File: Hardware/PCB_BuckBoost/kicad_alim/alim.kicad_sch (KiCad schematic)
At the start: 36 parts, among them J1 Conn_01x02, J2 Conn_01x02, J3 Conn_01x02, J4 Conn_01x02, U1 MIC3172YM, U2 MIC3172YM

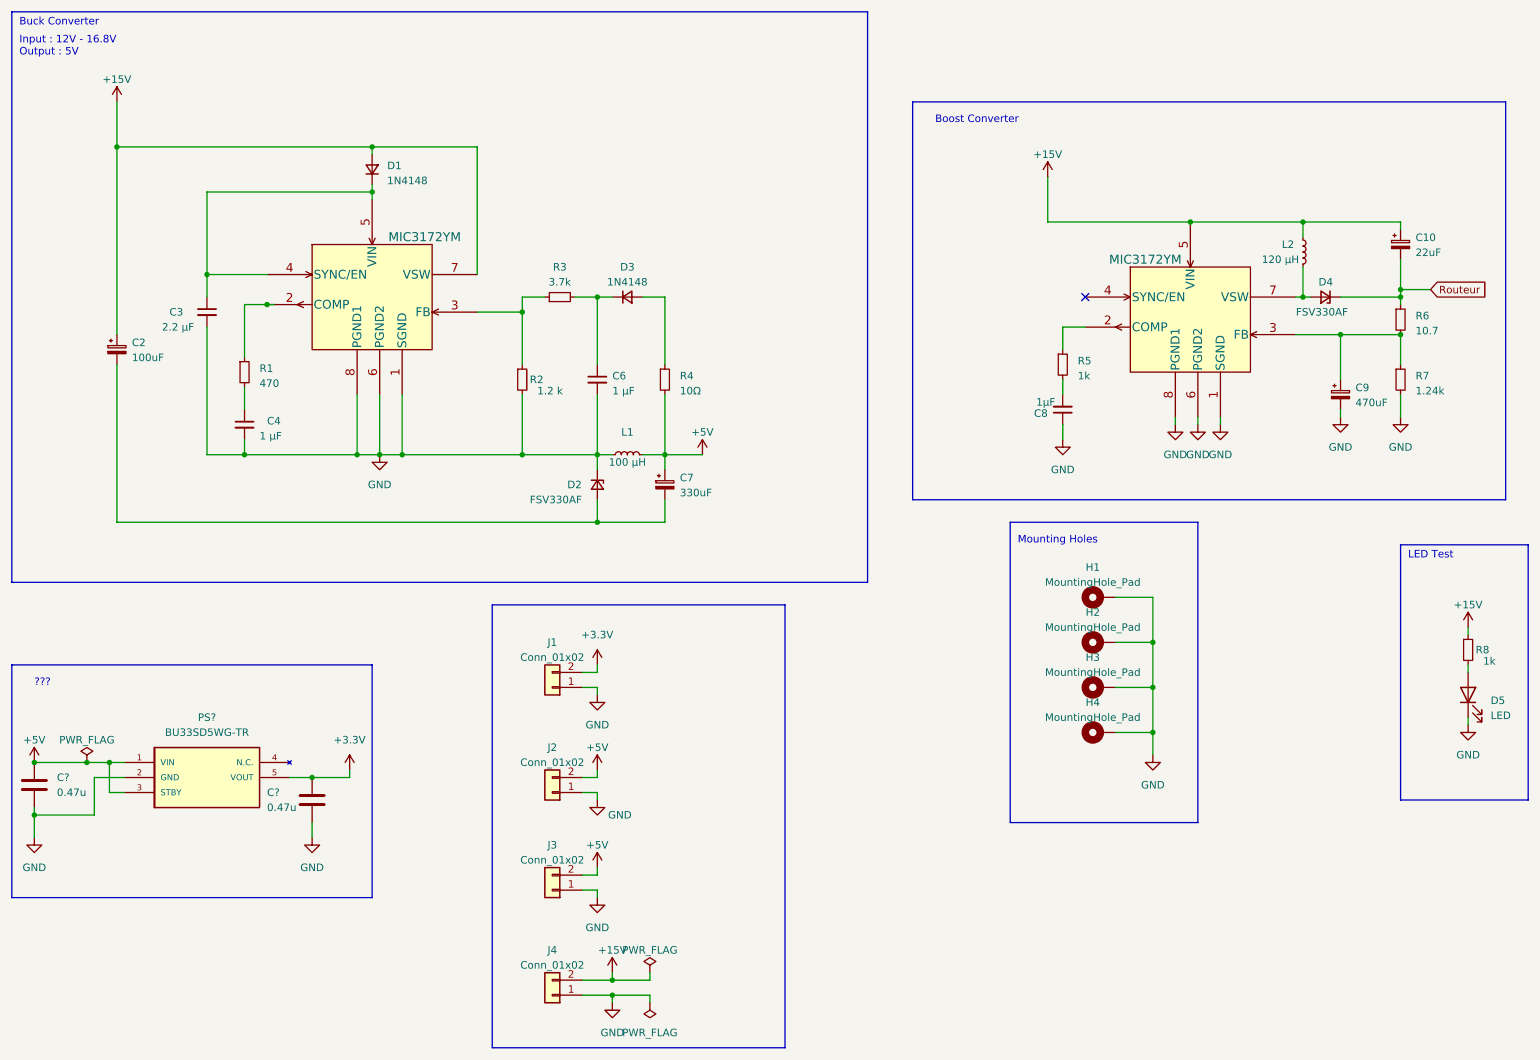
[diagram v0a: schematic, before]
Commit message: changement du schéma Buck/Boost car erreur
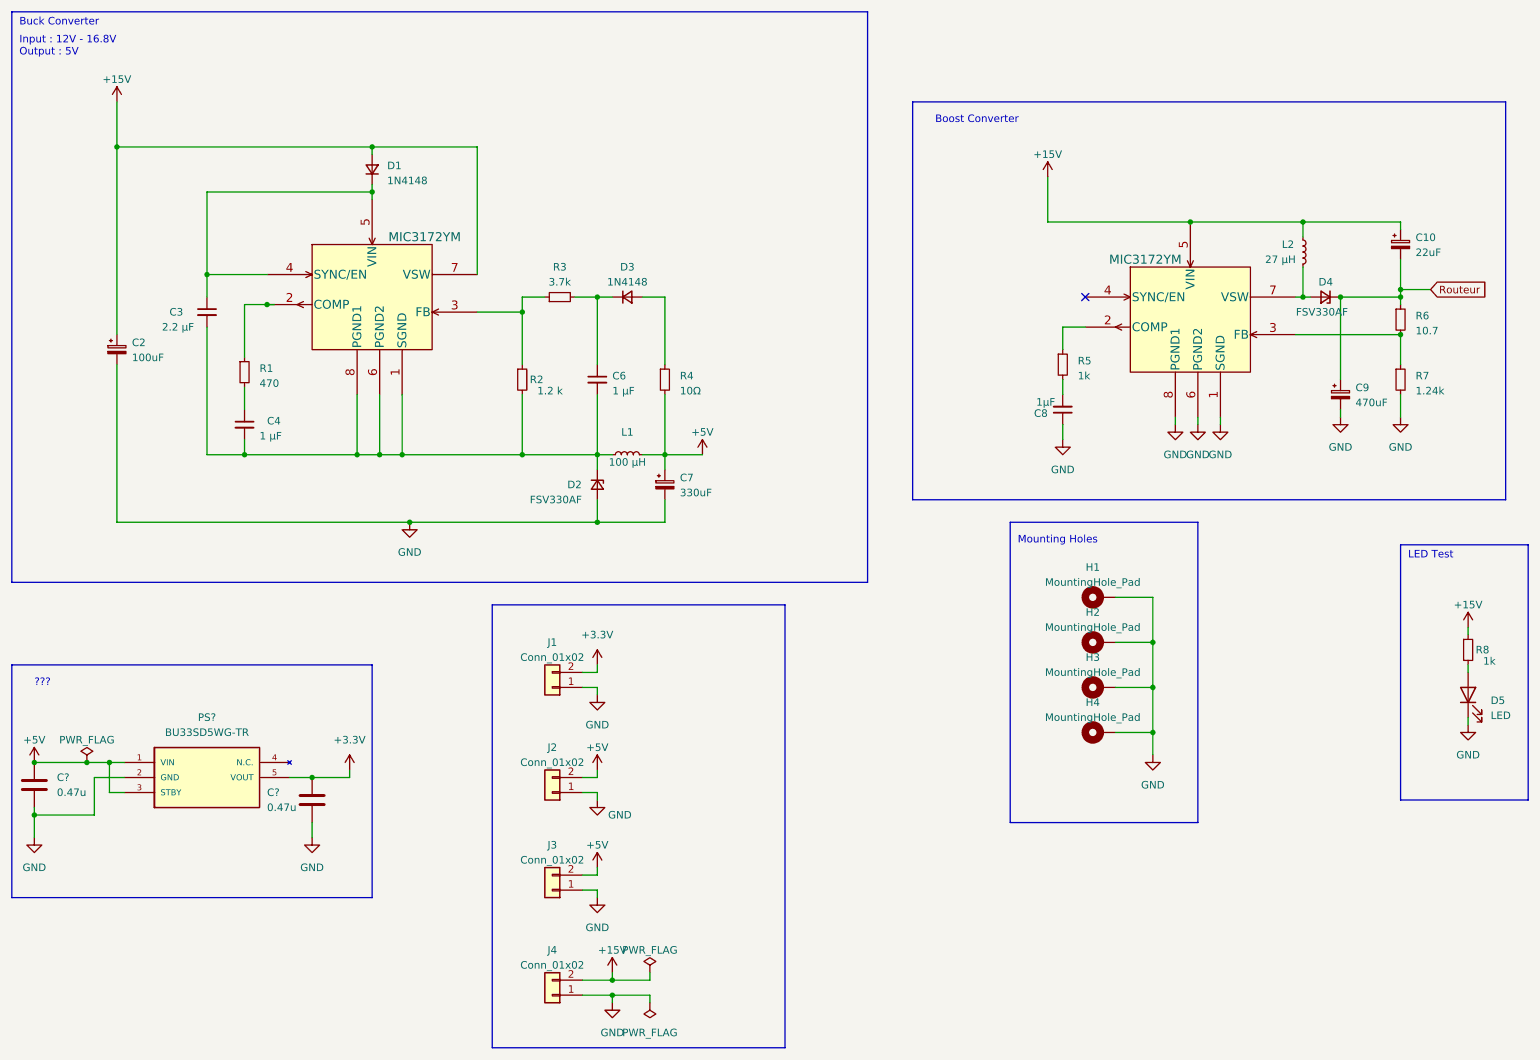
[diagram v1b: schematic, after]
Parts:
- L2: value 120 µH -> 27 µH
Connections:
- net GND: now also C2.2, C7.2, D2.2 (A); no longer C3.2, C4.2, C6.2, D2.1 (K), L1.1, R2.2, U1.1 (SGND), U1.6 (PGND2), U1.8 (PGND1)
- net Routeur: now also C9.1
- net at R6.2, R7.1, U2.3 (FB): no longer C9.1
- new net: C3.2, C4.2, C6.2, D2.1 (K), L1.1, R2.2, U1.1 (SGND), U1.6 (PGND2), U1.8 (PGND1)
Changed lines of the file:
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@@
   (junction (at 114.3 69.85) (diameter 0) (color 0 0 0 0)
   )
-  (junction (at 240.03 76.2) (diameter 0) (color 0 0 0 0)
-  )
   (junction (at 250.19 68.58) (diameter 0) (color 0 0 0 0)
   )
@@
   (junction (at 76.2 52.07) (diameter 0) (color 0 0 0 0)
   )
+  (junction (at 82.55 107.95) (diameter 0) (color 0 0 0 0)
+  )
   (junction (at 58.42 71.12) (diameter 0) (color 0 0 0 0)
   )
@@
   )
   (junction (at 27.94 148.59) (diameter 0) (color 0 0 0 0)
+  )
+  (junction (at 240.03 69.85) (diameter 0) (color 0 0 0 0)
   )
   (junction (at 77.47 96.52) (diameter 0) (color 0 0 0 0)
@@
     (stroke (width 0) (type default))
   )
-  (wire (pts (xy 240.03 76.2) (xy 250.19 76.2))
-    (stroke (width 0) (type default))
-  )
   (wire (pts (xy 193.04 91.44) (xy 193.04 93.98))
     (stroke (width 0) (type default))
@@
     (stroke (width 0) (type default))
   )
-  (wire (pts (xy 240.03 83.82) (xy 240.03 76.2))
-    (stroke (width 0) (type default))
-  )
   (wire (pts (xy 27.94 148.59) (xy 31.75 148.59))
     (stroke (width 0) (type default))
@@
     (stroke (width 0) (type default))
   )
+  (wire (pts (xy 240.03 69.85) (xy 240.03 83.82))
+    (stroke (width 0) (type default))
+  )
+  (wire (pts (xy 82.55 107.95) (xy 114.3 107.95))
+    (stroke (width 0) (type default))
+  )
   (wire (pts (xy 48.26 52.07) (xy 76.2 52.07))
     (stroke (width 0) (type default))
@@
     (stroke (width 0) (type default))
   )
-  (wire (pts (xy 232.41 76.2) (xy 240.03 76.2))
+  (wire (pts (xy 232.41 76.2) (xy 250.19 76.2))
     (stroke (width 0) (type default))
   )
@@
     (stroke (width 0) (type default))
   )
-  (wire (pts (xy 33.02 107.95) (xy 114.3 107.95))
+  (wire (pts (xy 33.02 107.95) (xy 82.55 107.95))
     (stroke (width 0) (type default))
   )
@@
       (effects (font (size 1.27 1.27)))
     )
-    (property "Value" "120 µH" (at 229.87 63.5 0)
+    (property "Value" "27 µH" (at 229.87 63.5 0)
       (effects (font (size 1.27 1.27)))
     )
@@
         (path "/9ea535e2-254b-400e-a1b3-21cc38003798"
           (reference "#PWR01") (unit 1)
-        )
-      )
-    )
-  )
-  (symbol (lib_id "power:GND") (at 77.47 96.52 0) (unit 1)
-    (in_bom yes) (on_board yes) (dnp no) (fields_autoplaced)
-    (property "Reference" "#PWR06" (at 77.47 102.87 0)
-      (effects (font (size 1.27 1.27)) hide)
-    )
-    (property "Value" "GND" (at 77.47 101.6 0)
-      (effects (font (size 1.27 1.27)))
-    )
-    (property "Footprint" "" (at 77.47 96.52 0)
-      (effects (font (size 1.27 1.27)) hide)
-    )
-    (property "Datasheet" "" (at 77.47 96.52 0)
-      (effects (font (size 1.27 1.27)) hide)
-    )
-    (pin "1")
-    (instances
-      (project "alim"
-        (path "/9ea535e2-254b-400e-a1b3-21cc38003798"
-          (reference "#PWR06") (unit 1)
         )
       )
@@
         )
       )
+    )
+  )
+  (symbol (lib_id "power:GND") (at 82.55 107.95 0) (unit 1)
+    (in_bom yes) (on_board yes) (dnp no) (fields_autoplaced)
+    (property "Reference" "#PWR06" (at 82.55 114.3 0)
+      (effects (font (size 1.27 1.27)) hide)
+    )
+    (property "Value" "GND" (at 82.55 113.03 0)
+      (effects (font (size 1.27 1.27)))
+    )
+    (property "Footprint" "" (at 82.55 107.95 0)
+      (effects (font (size 1.27 1.27)) hide)
+    )
+    (property "Datasheet" "" (at 82.55 107.95 0)
+      (effects (font (size 1.27 1.27)) hide)
+    )
+    (pin "1")
+    (instances
+      (project "alim"
+        (path "/9ea535e2-254b-400e-a1b3-21cc38003798"
+          (reference "#PWR06") (unit 1)
+        )
+      )

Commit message: Footprint Diode Shottky
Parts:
- D2: footprint Footprints_Balise:DO-214AD_ONS -> Custom:Diode_Shottky
- D4: footprint Footprints_Balise:DIODE_1N5822-T_DIO -> Custom:Diode_Shottky
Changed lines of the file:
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@@
       (effects (font (size 1.27 1.27)) (justify left))
     )
-    (property "Footprint" "Footprints_Balise:DO-214AD_ONS" (at 114.3 101.6 90)
+    (property "Footprint" "Custom:Diode_Shottky" (at 114.3 101.6 90)
       (effects (font (size 1.27 1.27)) hide)
     )
@@
       (effects (font (size 1.27 1.27)) (justify left))
     )
-    (property "Footprint" "Footprints_Balise:DIODE_1N5822-T_DIO" (at 237.49 69.85 90)
-      (effects (font (size 1.27 1.27)) hide)
-    )
+    (property "Footprint" "Custom:Diode_Shottky" (at 237.49 69.85 90)
+      (effects (font (size 1.27 1.27)) hide)
+    )
